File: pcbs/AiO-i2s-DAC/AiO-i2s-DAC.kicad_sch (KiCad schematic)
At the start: 47 parts, among them J1 UART1, J2 SJ-3524-SMT-TR-PI, J3 Audio Out, J4 UART0, Q3 BC818, Q4 MBT3904DW1, Q6 MBT3904DW1, U1 ESP32 A1S, U2 AZ1117CH-3.3TRG1

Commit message: PCM5102A implementation (initial schematics)
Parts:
- removed C4, C5: 0.1uF 50V, Capacitor_SMD:C_0603_1608Metric, symbol Device:C_Small
- removed R10, R11, R31: 0R, Resistor_SMD:R_0603_1608Metric, symbol Device:R_Small
- removed R8, R9: 22R 1%, Resistor_SMD:R_0603_1608Metric, symbol Device:R_Small
- removed U1: ESP32 A1S, PCM_Espressif:ESP32-WROVER-E_ThermalVias, symbol DIY:ESP32_A1S
- added C17, C20: 2.2uF, symbol Device:C_Small
- added C18, C22, C23, C25: 0.1uF 50V, Capacitor_SMD:C_0603_1608Metric, symbol Device:C_Small
- added C19, C21, C24, C26: 10uF 10V, Capacitor_SMD:C_0603_1608Metric, symbol Device:C_Small
- added C27, C28: 2.2nF, symbol Device:C_Small
- added FB1: FerriteBead_Small, symbol Device:FerriteBead_Small
- added R3, R4: 470, symbol Device:R_Small
- added R36, R37, R38, R39, R40: 10K 1%, Resistor_SMD:R_0603_1608Metric, symbol Device:R_Small
- added R41: 0R, Resistor_SMD:R_0603_1608Metric, symbol Device:R_Small
- added U1: ESP32-WROVER-E, PCM_Espressif:ESP32-WROVER-E, symbol PCM_Espressif:ESP32-WROVER-E
- added U5: PCM5102A, Package_SO:TSSOP-20_4.4x6.5mm_P0.65mm, symbol Audio:PCM5102A
- J2: value SJ-3524-SMT-TR-PI -> SJ-3524-SMT-TR; Arrow Part Number SJ-3524-SMT-TR-PI -> SJ-3524-SMT-TR; Arrow Price/Stock https://www.arrow.com/en/products/sj-3524-smt-tr-pi/cui-dev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 -> (none); Manufacturer_Part_Number SJ-3524-SMT-TR-PI -> SJ-3524-SMT-TR; Mouser Part Number 490-SJ3524SMTTRPI -> 490-SJ-3524-SMT-TR; Mouser Price/Stock https://www.mouser.co.uk/ProductDetail/Same-Sky/SJ-3524-SMT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 -> (none)
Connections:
- net AGND is gone; now on net GND: J2.S, J3.1 (Pin_1)
- net +3.3V: now also FB1.1, R39.1, R41.2, U1.2 (3V3)
- net EN: now also U1.3 (EN/CHIP_PU)
- net GND: now also C17.1, C18.1, C19.2, C21.2, C22.1, C23.1, C24.2, C25.1, C26.2, C27.2, C28.2, R36.2, R37.2, R38.2, R40.2, U1.1 (GND), U1.15 (GND), U1.38 (GND), U1.39 (GND_THERMAL), U5.19 (DGND), U5.3 (CPGND), U5.9 (AGND)
- net IO0: now also U1.25 (GPIO0/BOOT/ADC2_CH1)
- net IO18: now also U1.30 (GPIO18)
- net IO2: now also U1.24 (ADC2_CH2/GPIO2)
- net IO5: now also U1.29 (GPIO5)
- net LOUT: now also C27.1, R3.2
- net ROUT: now also C28.1, R4.1
- net RXD0: now also U1.34 (U0RXD/GPIO3)
- net RXD1: now also U1.31 (GPIO19)
- net TXD0: now also U1.35 (U0TXD/GPIO1)
- net TXD1: now also U1.33 (GPIO21)
- net at JP2.1 (A): now also U1.23 (MTDO/GPIO15/ADC2_CH3)
- new net: C18.2, C19.1, U5.18 (LDOO)
- new net: C20.1, U5.2 (CAPP)
- new net: C20.2, U5.4 (CAPM)
- new net: C17.2, U5.5 (VNEG)
- new net: R3.1, U5.6 (OUTL)
- new net: R4.2, U5.7 (OUTR)
- new net AVDD: C21.1, C22.2, C25.2, C26.1, FB1.2, U5.1 (CPVDD), U5.8 (AVDD)
- new net BCLK: U1.12 (ADC2_CH7/GPIO27), U5.13 (BCK)
- new net DEMPH: R38.1, U5.10 (DEMP)
- new net DIN: U1.11 (DAC_2/ADC2_CH9/GPIO26), U5.14 (DIN)
- new net DVDD: C23.2, C24.1, R41.1, U5.20 (DVDD)
- new net FILTER: R37.1, U5.11 (FLT)
- new net FORMAT: R40.1, U5.16 (FMT)
- new net MUTE: R39.2, U5.17 (XSMT)
- new net SCK_IN: R36.1, U5.12 (SCK)
- new net WSEL: U1.10 (DAC_1/ADC2_CH8/GPIO25), U5.15 (LRCK)
- no-connect marks 30 -> 9
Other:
- title: A1S Mini Board -> AiO-i2s-DAC
- moved on the sheet: 3V1, 5V1, C1, C16, C2, C3, C6, C7, C8, C9, D5, D6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

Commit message: BOM pre-fill, no layout
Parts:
- removed C19: 10uF 10V, Capacitor_SMD:C_0603_1608Metric, symbol Device:C_Small
- added C29: 10uF 16V, Capacitor_SMD:C_0805_2012Metric, symbol Device:C_Small
- added JP3: SolderJumper_2_Bridged, Jumper:SolderJumper-2_P1.3mm_Bridged_RoundedPad1.0x1.5mm, symbol Jumper:SolderJumper_2_Bridged
- C17, C20: value 2.2uF -> 2.2uF 16V; footprint (none) -> Capacitor_SMD:C_0603_1608Metric; Manufacturer_Name (none) -> amsung Electro-Mechanics; Manufacturer_Part_Number (none) -> CL10A225KO8NNNC
- C21, C24, C26: value 10uF 10V -> 10uF 16V; footprint Capacitor_SMD:C_0603_1608Metric -> Capacitor_SMD:C_0805_2012Metric; Manufacturer_Part_Number CL10A106KP8NNNC -> CL21A106KOQNNNG
- C27, C28: footprint (none) -> Capacitor_SMD:C_0603_1608Metric; Manufacturer_Name (none) -> YAGEO; Manufacturer_Part_Number (none) -> CC0603KRX7R9BB222
- FB1: now not fitted; now left out of the parts list
- R3, R4: value 470 -> 470R 1%; footprint (none) -> Resistor_SMD:R_0603_1608Metric; Manufacturer_Name (none) -> YAGEO; Manufacturer_Part_Number (none) -> RC0603FR-07470RL
- U1: Manufacturer_Name (none) -> Espressif Systems; Manufacturer_Part_Number (none) -> ESP32-WROVER-E-N4R8
- U5: Manufacturer_Name (none) -> Texas Instruments; Manufacturer_Part_Number (none) -> PCM5102APWR
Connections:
- net +3.3V: now also JP3.2 (B)
- net AVDD: now also JP3.1 (A)
- net GND: now also C29.2
- net at C18.2, U5.18 (LDOO): now also C29.1

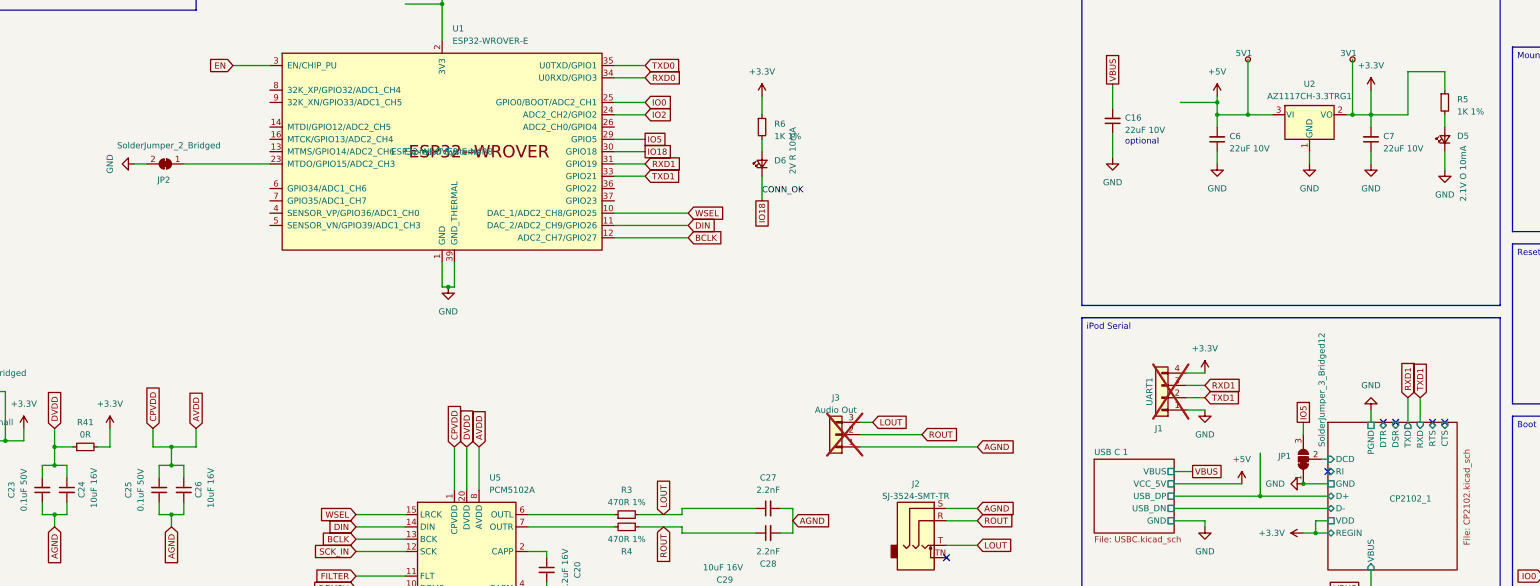
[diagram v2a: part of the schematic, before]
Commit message: Exposing DCD, 3V3 and 5V in schematic
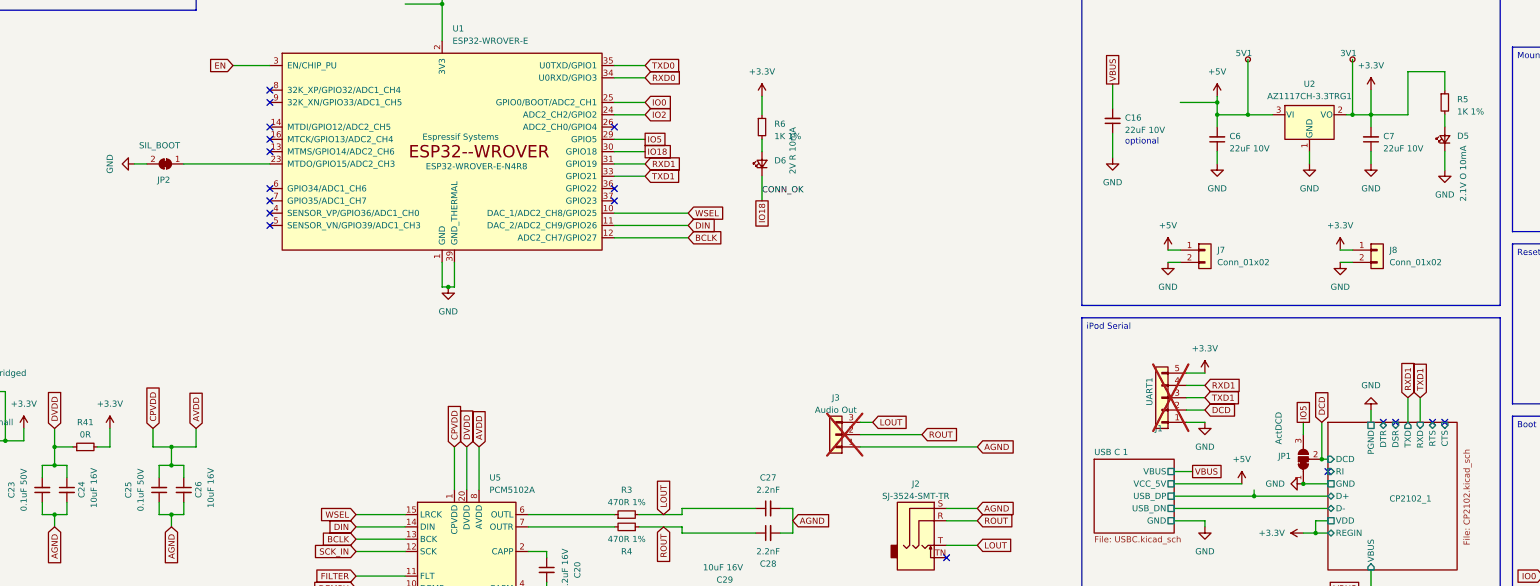
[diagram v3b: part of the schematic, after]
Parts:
- added J7, J8: Conn_01x02, Connector_PinHeader_2.54mm:PinHeader_1x02_P2.54mm_Vertical, symbol Connector_Generic:Conn_01x02
- J1: symbol Connector_Generic:Conn_01x04 -> Connector_Generic:Conn_01x05; now in the parts list
- JP1: value SolderJumper_3_Bridged12 -> ActDCD
- JP2: value SolderJumper_2_Bridged -> SIL_BOOT
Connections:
- net +3.3V: now also J1.5 (Pin_5), J8.1 (Pin_1); no longer J1.4 (Pin_4)
- net +5V: now also J7.1 (Pin_1)
- net GND: now also J7.2 (Pin_2), J8.2 (Pin_2)
- net RXD1: now also J1.4 (Pin_4); no longer J1.3 (Pin_3)
- net TXD1: now also J1.3 (Pin_3); no longer J1.2 (Pin_2)
- net CP2102_1/DCD renamed DCD
- net DCD: now also J1.2 (Pin_2)
- no-connect marks 9 -> 21

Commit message: Footprints update
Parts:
- J1: footprint Connector_PinHeader_2.54mm:PinHeader_1x04_P2.54mm_Vertical -> Connector_PinHeader_2.54mm:PinHeader_1x05_P2.54mm_Vertical
- U1: footprint PCM_Espressif:ESP32-WROVER-E -> PCM_Espressif:ESP32-WROVER-E_ThermalVias
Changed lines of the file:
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@@
 		(exclude_from_sim yes)
 		(in_bom no)
-		(on_board yes)
+		(on_board no)
 		(dnp yes)
 		(fields_autoplaced yes)
@@
 			)
 		)
-		(property "Footprint" "Connector_PinHeader_2.54mm:PinHeader_1x04_P2.54mm_Vertical"
+		(property "Footprint" "Connector_PinHeader_2.54mm:PinHeader_1x05_P2.54mm_Vertical"
 			(at 279.4 129.54 0)
 			(effects
@@
 			)
 		)
-		(property "Footprint" "PCM_Espressif:ESP32-WROVER-E"
+		(property "Footprint" "PCM_Espressif:ESP32-WROVER-E_ThermalVias"
 			(at 133.35 111.76 0)
 			(effects

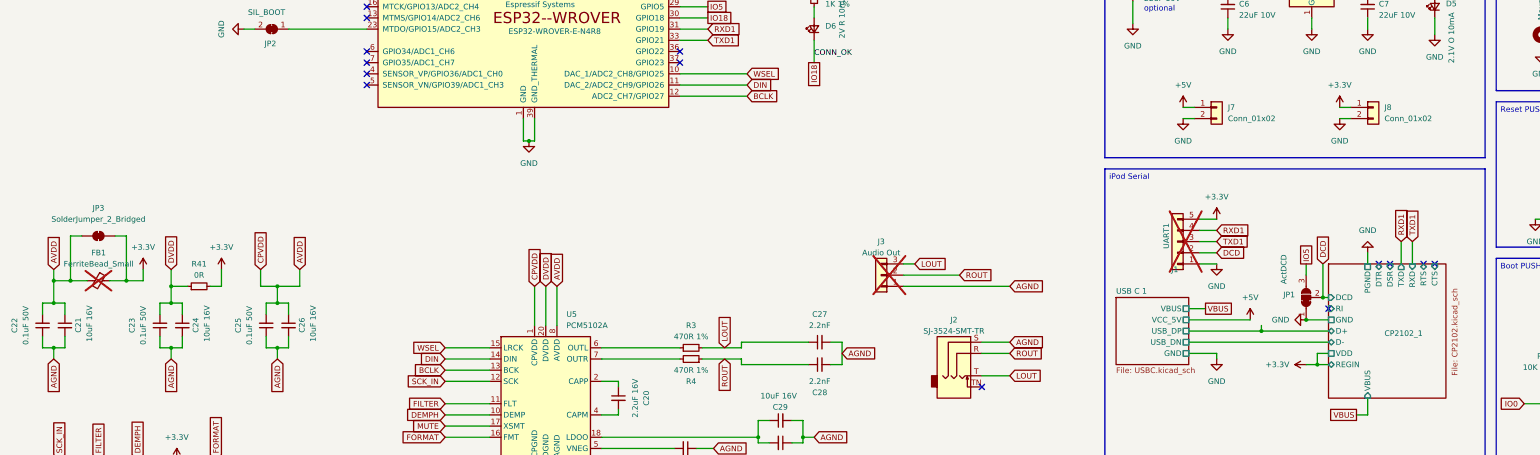
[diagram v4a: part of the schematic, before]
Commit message: CP2102 instead of CP2102N
Moving some components to CP2102 non N
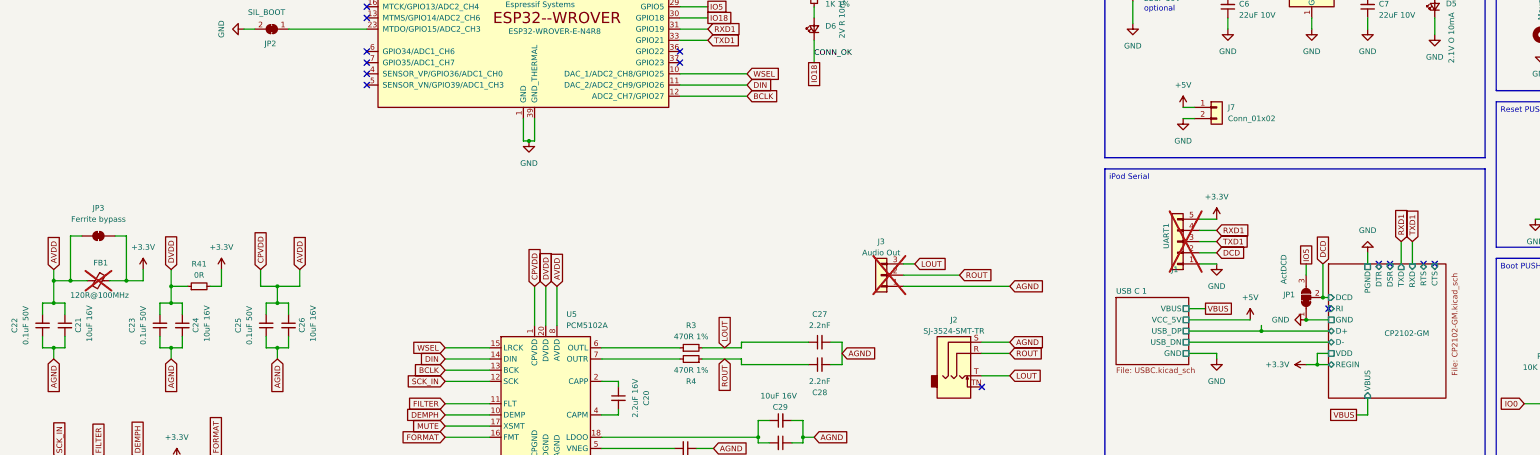
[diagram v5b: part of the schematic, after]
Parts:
- removed J8: Conn_01x02, Connector_PinHeader_2.54mm:PinHeader_1x02_P2.54mm_Vertical, symbol Connector_Generic:Conn_01x02
- FB1: value FerriteBead_Small -> 120R@100MHz; footprint (none) -> Inductor_SMD:L_0603_1608Metric; Manufacturer_Name (none) -> TDK Corporation; Manufacturer_Part_Number (none) -> MAF1608GAD601CT000
- JP3: value SolderJumper_2_Bridged -> Ferrite bypass; footprint Jumper:SolderJumper-2_P1.3mm_Bridged_RoundedPad1.0x1.5mm -> Jumper:SolderJumper-2_P1.3mm_Open_RoundedPad1.0x1.5mm
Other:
- sheet CP2102_1 renamed CP2102-GM
- sheet CP2102-GM: file CP2102.kicad_sch -> CP2102-GM.kicad_sch
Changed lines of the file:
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@@
 	(title_block
 		(title "AiO-i2s-DAC")
-		(date "2025-05-18")
-		(rev "0.1.2")
+		(date "2025-05-26")
+		(rev "0.1.4")
 		(company "Martin Roger")
 	)
@@
 	(wire
 		(pts
-			(xy 316.23 99.06) (xy 318.77 99.06)
-		)
-		(stroke
-			(width 0)
-			(type default)
-		)
-	)
-	(wire
-		(pts
 			(xy 25.4 179.07) (xy 25.4 182.88)
 		)
@@
 	(wire
 		(pts
-			(xy 316.23 101.6) (xy 318.77 101.6)
-		)
-		(stroke
-			(width 0)
-			(type default)
-		)
-	)
-	(wire
-		(pts
 			(xy 24.13 143.51) (xy 26.67 143.51)
 		)
@@
 	)
 	(symbol
-		(lib_id "power:GND")
-		(at 316.23 101.6 0)
-		(unit 1)
-		(exclude_from_sim no)
-		(in_bom yes)
-		(on_board yes)
-		(dnp no)
-		(fields_autoplaced yes)
-		(property "Reference" "#PWR056"
-			(at 316.23 107.95 0)
-			(effects
-				(font
-					(size 1.27 1.27)
-				)
-				(hide yes)
-			)
-		)
-		(property "Value" "GND"
-			(at 316.23 106.68 0)
-			(effects
-				(font
-					(size 1.27 1.27)
-				)
-			)
-		)
-		(property "Footprint" ""
-			(at 316.23 101.6 0)
-			(effects
-				(font
-					(size 1.27 1.27)
-				)
-				(hide yes)
-			)
-		)
-		(property "Datasheet" ""
-			(at 316.23 101.6 0)
-			(effects
-				(font
-					(size 1.27 1.27)
-				)
-				(hide yes)
-			)
-		)
-		(property "Description" ""
-			(at 316.23 101.6 0)
-			(effects
-				(font
-					(size 1.27 1.27)
-				)
-			)
-		)
-		(pin "1"
-		)
-		(instances
-			(project "AiO-i2s-DAC"
-				(path "/473bba75-08f8-4c6c-a9b2-aa3e95e63a5e"
-					(reference "#PWR056")
-					(unit 1)
-				)
-			)
-		)
-	)
-	(symbol
 		(lib_id "Connector:TestPoint_Small")
 		(at 308.61 209.55 270)
@@
 		(exclude_from_sim yes)
 		(in_bom no)
-		(on_board no)
+		(on_board yes)
 		(dnp yes)
-		(fields_autoplaced yes)
 		(property "Reference" "FB1"
-			(at 34.3281 132.08 90)
+			(at 34.798 134.366 90)
 			(effects
 				(font
@@
 			)
 		)
-		(property "Value" "FerriteBead_Small"
-			(at 34.3281 134.62 90)
+		(property "Value" "120R@100MHz"
+			(at 34.544 141.732 90)
 			(effects
 				(font
@@
 			)
 		)
-		(property "Footprint" ""
+		(property "Footprint" "Inductor_SMD:L_0603_1608Metric"
 			(at 34.29 136.652 90)
 			(effects
@@
 			)
 		)
-		(property "Datasheet" "~"
+		(property "Datasheet" "https://product.tdk.com/en/system/files?file=dam/doc/product/emc/emc/suppression-filter/catalog/suppression-filter_commercial_maf1608g_en.pdf"
 			(at 34.29 138.43 0)
 			(effects
@@
 			)
 		)
-		(property "Description" "Ferrite bead, small symbol"
+		(property "Description" "FERRITE BEAD 120 OHM 0603 1LN"
 			(at 34.29 138.43 0)
 			(effects
@@
 			)
 		)
+		(property "Manufacturer_Name" "TDK Corporation"
+			(at 34.29 138.43 90)
+			(effects
+				(font
+					(size 1.27 1.27)
+				)
+				(hide yes)
+			)
+		)
+		(property "Manufacturer_Part_Number" "MAF1608GAD601CT000"
+			(at 34.29 138.43 90)
+			(effects
+				(font
+					(size 1.27 1.27)
+				)
+				(hide yes)
+			)
+		)
 		(pin "2"
 		)
@@
 	)
 	(symbol
-		(lib_id "power:+3.3V")
-		(at 316.23 99.06 0)
-		(unit 1)
-		(exclude_from_sim no)
-		(in_bom yes)
-		(on_board yes)
-		(dnp no)
-		(fields_autoplaced yes)
-		(property "Reference" "#PWR050"
-			(at 316.23 102.87 0)
-			(effects
-				(font
-					(size 1.27 1.27)
-				)
-				(hide yes)
-			)
-		)
-		(property "Value" "+3.3V"
-			(at 316.23 93.98 0)
-			(effects
-				(font
-					(size 1.27 1.27)
-				)
-			)
-		)
-		(property "Footprint" ""
-			(at 316.23 99.06 0)
-			(effects
-				(font
-					(size 1.27 1.27)
-				)
-				(hide yes)
-			)
-		)
-		(property "Datasheet" ""
-			(at 316.23 99.06 0)
-			(effects
-				(font
-					(size 1.27 1.27)
-				)
-				(hide yes)
-			)
-		)
-		(property "Description" ""
-			(at 316.23 99.06 0)
-			(effects
-				(font
-					(size 1.27 1.27)
-				)
-			)
-		)
-		(pin "1"
-		)
-		(instances
-			(project "AiO-i2s-DAC"
-				(path "/473bba75-08f8-4c6c-a9b2-aa3e95e63a5e"
-					(reference "#PWR050")
-					(unit 1)
-				)
-			)
-		)
-	)
-	(symbol
 		(lib_id "Device:C_Small")
 		(at 377.19 154.94 180)
@@
 			)
 		)
-		(property "Value" "SolderJumper_2_Bridged"
+		(property "Value" "Ferrite bypass"
 			(at 34.29 124.46 0)
 			(effects
@@
 			)
 		)
-		(property "Footprint" "Jumper:SolderJumper-2_P1.3mm_Bridged_RoundedPad1.0x1.5mm"
+		(property "Footprint" "Jumper:SolderJumper-2_P1.3mm_Open_RoundedPad1.0x1.5mm"
 			(at 34.29 128.27 0)
 			(effects
@@
 	)
 	(symbol
-		(lib_id "Connector_Generic:Conn_01x02")
-		(at 323.85 99.06 0)
-		(unit 1)
-		(exclude_from_sim no)
-		(in_bom yes)
-		(on_board yes)
-		(dnp no)
-		(fields_autoplaced yes)
-		(property "Reference" "J8"
-			(at 326.39 99.0599 0)
-			(effects
-				(font
-					(size 1.27 1.27)
-				)
-				(justify left)
-			)
-		)
-		(property "Value" "Conn_01x02"
-			(at 326.39 101.5999 0)
-			(effects
-				(font
-					(size 1.27 1.27)
-				)
-				(justify left)
-			)
-		)
-		(property "Footprint" "Connector_PinHeader_2.54mm:PinHeader_1x02_P2.54mm_Vertical"
-			(at 323.85 99.06 0)
-			(effects
-				(font
-					(size 1.27 1.27)
-				)
-				(hide yes)
-			)
-		)
-		(property "Datasheet" "~"
-			(at 323.85 99.06 0)
-			(effects
-				(font
-					(size 1.27 1.27)
-				)
-				(hide yes)
-			)
-		)
-		(property "Description" "Generic connector, single row, 01x02, script generated (kicad-library-utils/schlib/autogen/connector/)"
-			(at 323.85 99.06 0)
-			(effects
-				(font
-					(size 1.27 1.27)
-				)
-				(hide yes)
-			)
-		)
-		(pin "1"
-		)
-		(pin "2"
-		)
-		(instances
-			(project "AiO-i2s-DAC"
-				(path "/473bba75-08f8-4c6c-a9b2-aa3e95e63a5e"
-					(reference "J8")
-					(unit 1)
-				)
-			)
-		)
-	)
-	(symbol
 		(lib_id "Device:R_Small")
 		(at 391.16 156.21 0)
@@
 			(color 0 0 0 0.0000)
 		)
-		(property "Sheetname" "CP2102_1"
+		(property "Sheetname" "CP2102-GM"
 			(at 326.39 151.13 0)
 			(effects
@@
 			)
 		)
-		(property "Sheetfile" "CP2102.kicad_sch"
+		(property "Sheetfile" "CP2102-GM.kicad_sch"
 			(at 341.63 160.02 90)
 			(effects
